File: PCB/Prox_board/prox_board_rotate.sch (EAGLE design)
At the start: 7 parts, among them U1 MAX44000

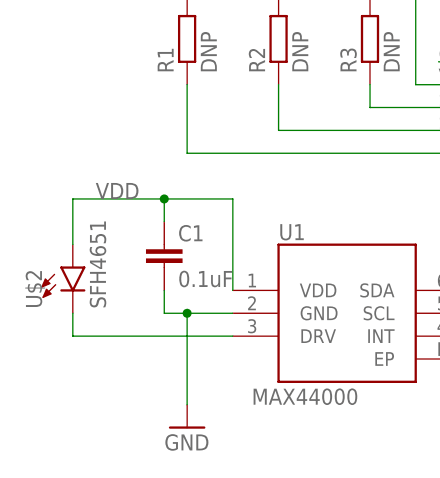
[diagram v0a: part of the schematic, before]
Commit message: Fix naming and silkscreen on the back of the board!
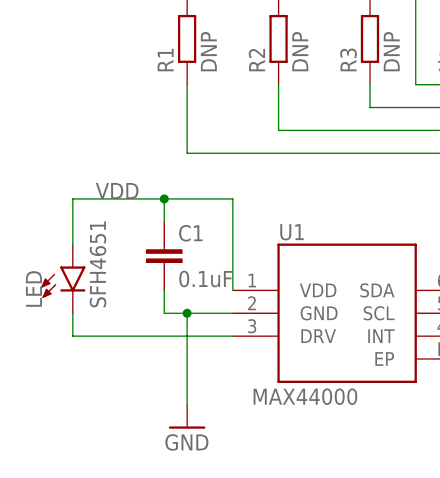
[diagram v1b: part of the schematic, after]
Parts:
- renumbered U$2 to LED
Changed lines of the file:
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@@
 <parts>
 <part name="U1" library="Wisp5_Harvester_Motor-driver_V2" deviceset="MAX44000" device=""/>
-<part name="U$2" library="Wisp5_Harvester_Motor-driver_V2" deviceset="SFH4651" device=""/>
+<part name="LED" library="Wisp5_Harvester_Motor-driver_V2" deviceset="SFH4651" device=""/>
 <part name="JP1" library="Wisp5_Harvester_Motor-driver_V2" deviceset="PINHEAD_PINHD-1X5-1.27MM" device=""/>
 <part name="GND1" library="Wisp5_Harvester_Motor-driver" deviceset="GND" device=""/>
@@
 <instances>
 <instance part="U1" gate="G$1" x="35.56" y="17.78"/>
-<instance part="U$2" gate="G$1" x="5.08" y="22.86"/>
+<instance part="LED" gate="G$1" x="5.08" y="22.86"/>
 <instance part="JP1" gate="G$1" x="58.42" y="40.64"/>
 <instance part="GND1" gate="1" x="17.78" y="5.08"/>
@@
 <net name="N$1" class="0">
 <segment>
-<pinref part="U$2" gate="G$1" pin="C"/>
+<pinref part="LED" gate="G$1" pin="C"/>
 <wire x1="5.08" y1="17.78" x2="5.08" y2="15.24" width="0.1524" layer="91"/>
 <pinref part="U1" gate="G$1" pin="DRV"/>
@@
 <wire x1="15.24" y1="30.48" x2="22.86" y2="30.48" width="0.1524" layer="91"/>
 <label x="7.62" y="30.48" size="1.778" layer="95"/>
-<pinref part="U$2" gate="G$1" pin="A"/>
+<pinref part="LED" gate="G$1" pin="A"/>
 <wire x1="5.08" y1="25.4" x2="5.08" y2="30.48" width="0.1524" layer="91"/>
 <wire x1="5.08" y1="30.48" x2="15.24" y2="30.48" width="0.1524" layer="91"/>
